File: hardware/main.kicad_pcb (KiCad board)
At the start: 4 copper layers, 88 x 111 mm, 397 parts, among them J1 DS1128-09-S8B8X, J2 DS1128-09-S8B8X, J3 DS1128-09-S8B8X, J4 98424-G52-04ALF, J6 IDC-08M, J7 IDC-08M, J8 USB_C_Receptacle, J9 TYPE-C-31-M-12, Q1 SSM6J501NU, Q2 SSM6J501NU, Q3 FDV301N, Q4 BC817, SW1 TS-1187A-B-A-B, SW2 TS-1187A-B-A-B, SW3 TS-1187A-B-A-B, SW4 TS-1187A-B-A-B, U1 SN74LVC1G175, U10 W25Q256FVEIG, U12 TPD2EUSB30, U13 TPD2EUSB30, U14 TPD2EUSB30, U15 IP5328P, U16 N096-2864KSWEG01-H30, U2 MT7621A, U3 TPS63020, U4 TPS63020, U5 MT3420B, U6 MT3420B, U7 MT3420B, U8 MT3420B, U9 NT5CB64M16FP-DH (!), Y1 X322540MPB4SI

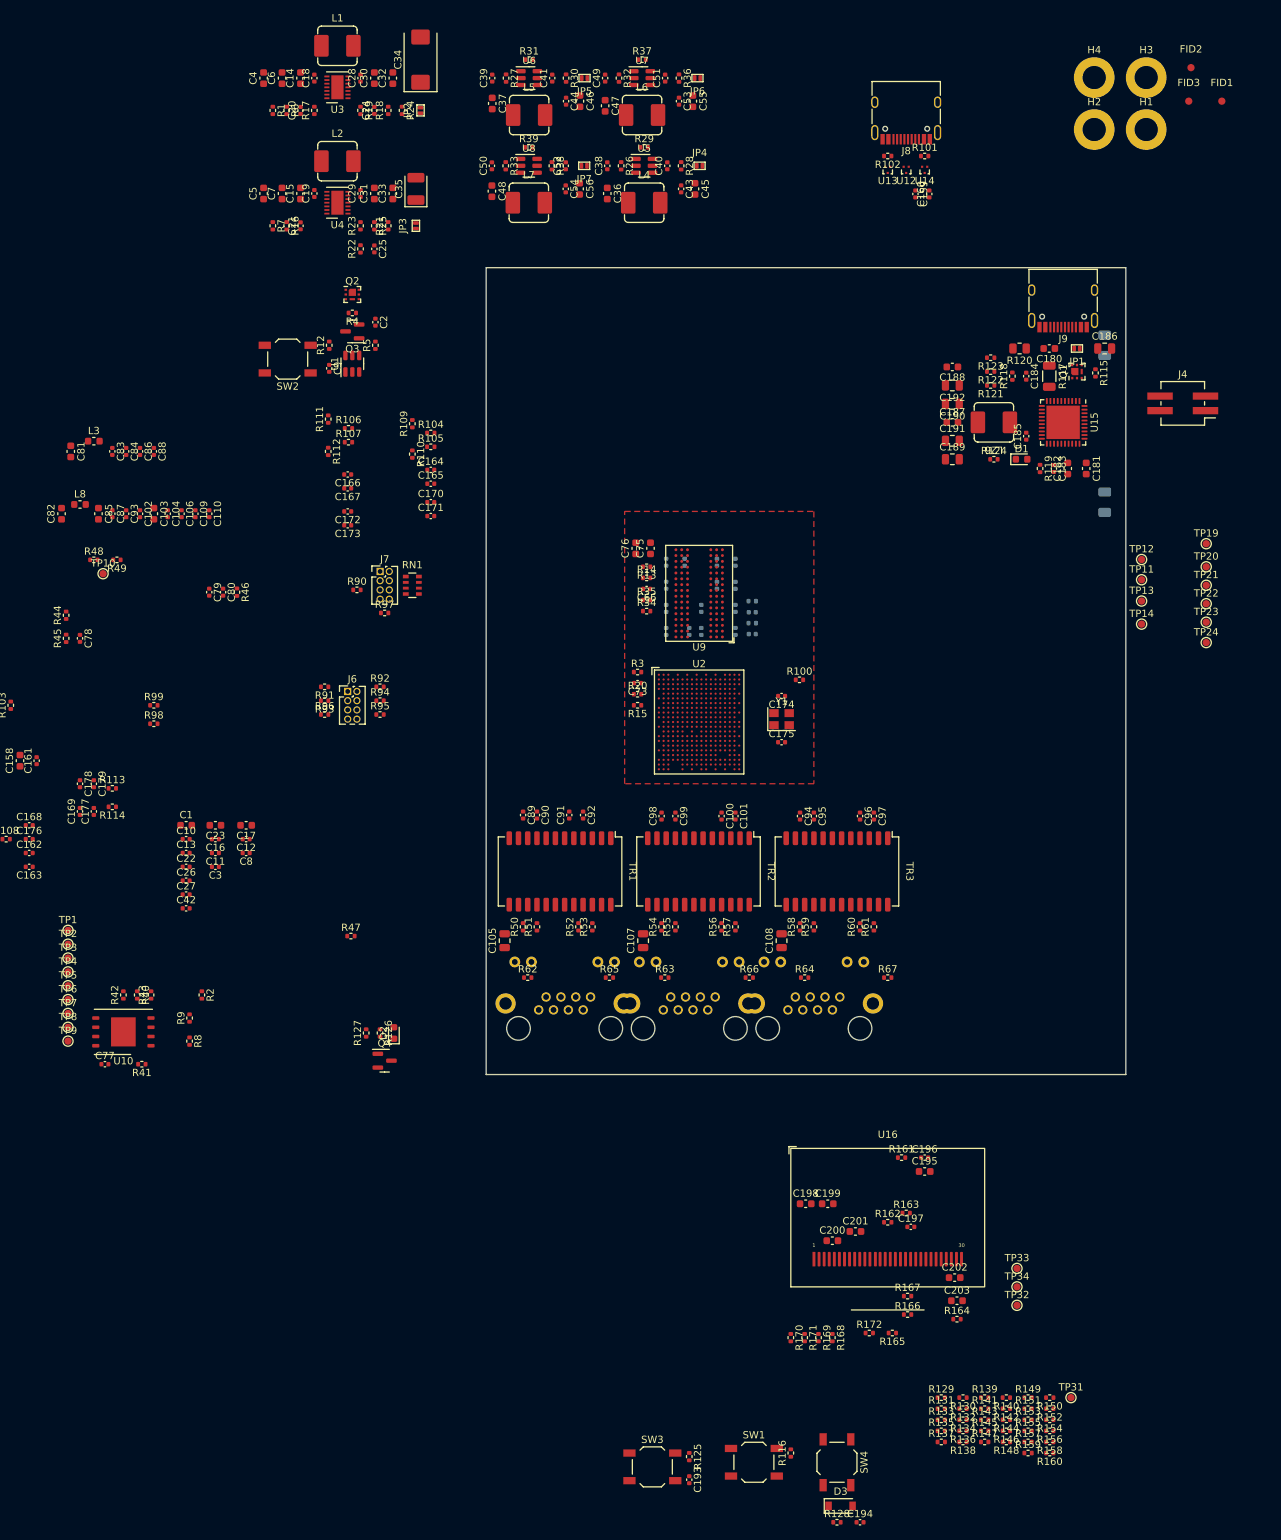
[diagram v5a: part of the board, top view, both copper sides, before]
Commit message: add mini-pcie and m2
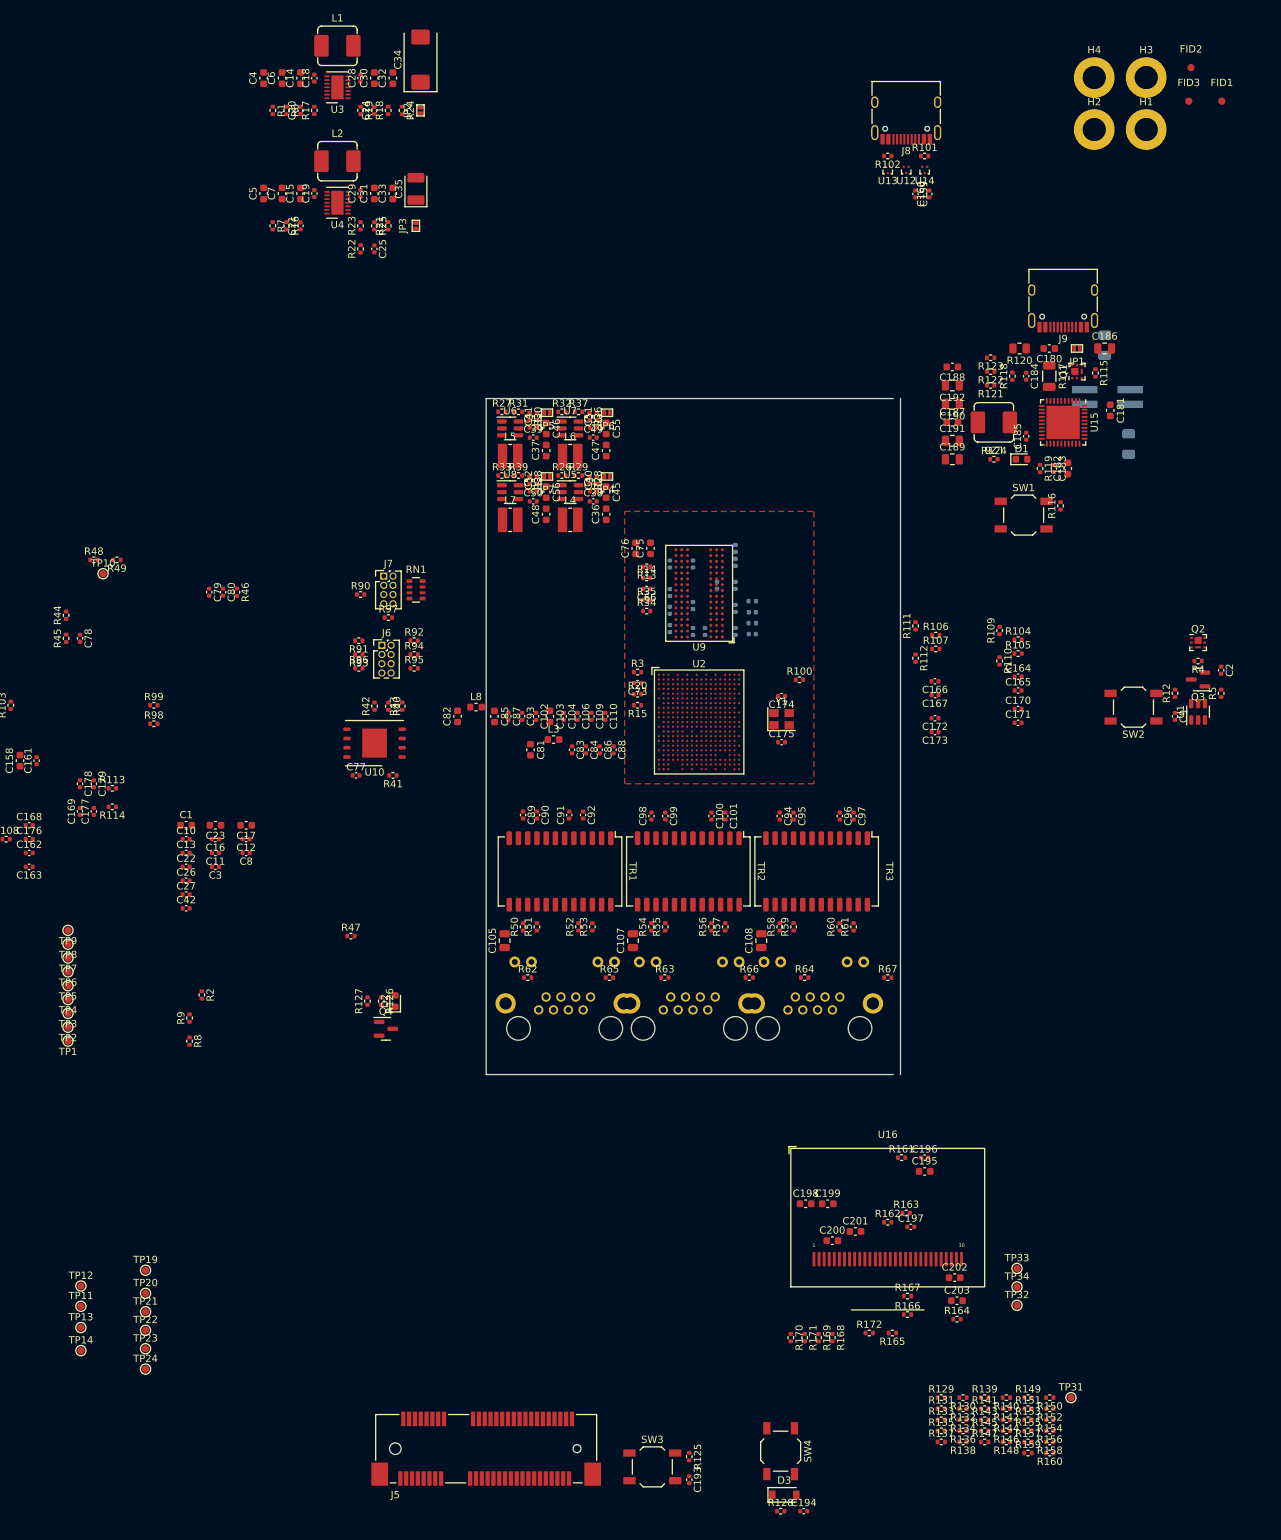
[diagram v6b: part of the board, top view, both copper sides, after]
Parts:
- added J5: Bus_PCI_Express_Mini, Connector_PCBEdge:BUS_PCI_Express_Mini_Dual, F.Cu at (0.00, 51.5)
- J4: moved to B.Cu
- L4, L5, L6, L7: value SLO0530H2R2MTT -> LVS303015-2R2M; footprint MAS_Package_std:Power_inductor_SMD_0530 -> Inductor_SMD:L_Wuerth_MAPI-3015
- moved TP11 176.9 mm to (-55.8, 31.9)
- moved TP12 176.9 mm to (-55.8, 29.1)
- moved TP13 176.9 mm to (-55.8, 34.8)
- moved TP14 176.9 mm to (-55.8, 38.0)
- moved TP19 176.9 mm to (-46.9, 26.9)
- moved TP20 176.9 mm to (-46.9, 30.1)
- moved TP21 176.9 mm to (-46.9, 32.6)
- moved TP22 176.9 mm to (-46.9, 35.2)
- moved TP23 176.9 mm to (-46.9, 37.7)
- moved TP24 176.9 mm to (-46.9, 40.5)
- moved SW1 135.5 mm to (73.9, -77.0)
- moved R116 135.5 mm to (79.0, -78.2)
- moved C2 125.8 mm to (101.1, -55.6)
- moved C9 125.8 mm to (94.8, -49.3)
- moved Q2 125.8 mm to (97.9, -59.4)
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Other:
- board size 88 x 111 mm -> 57 x 93 mm
